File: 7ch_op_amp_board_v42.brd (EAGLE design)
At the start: 10.5 x 15.2 mm, 12 parts

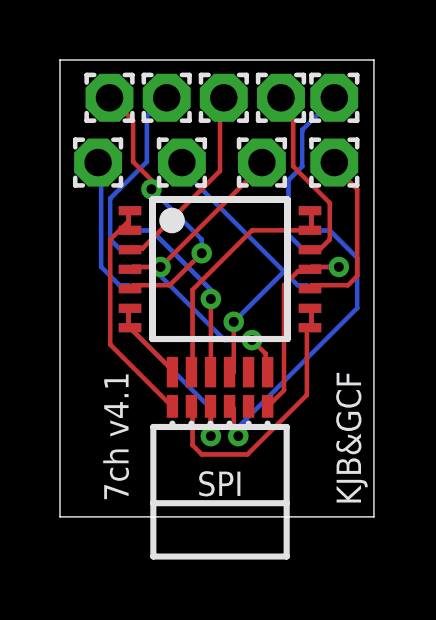
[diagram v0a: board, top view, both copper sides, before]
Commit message: Redraw traces to isolate power
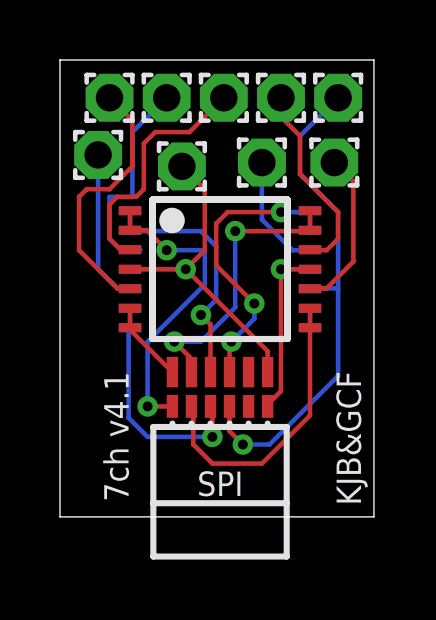
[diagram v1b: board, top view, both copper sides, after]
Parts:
- moved PAD8 5.64 mm to (9.27, 13.7)
- moved PAD7 3.24 mm to (6.73, 11.6)
- moved PAD9 2.67 mm to (4.06, 11.4)
- moved PAD5 0.25 mm to (1.27, 11.8)
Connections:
- net GND: now also SPI.B4; no longer SPI.T4
- net N$5: now also SPI.T4; no longer SPI.B4
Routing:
- net GND: track 10.4 -> 16.8 mm
- net N$1: track 7.96 -> 10.2 mm, vias 0 -> 2
- net N$21: track 6.11 -> 3.94 mm
- net N$5: track 11.4 -> 9.77 mm, vias 1 -> 3
- net N$8: track 6.64 -> 8.17 mm
- net N$3: track 6.40 -> 7.84 mm
- net N$4: track 6.95 -> 8.28 mm
- net N$7: track 8.19 -> 9.51 mm, vias 0 -> 2
- net N$9: track 9.02 -> 9.84 mm
- net N$22: track 6.33 -> 7.14 mm
- net V-: track 7.36 -> 6.73 mm
- net N$11: track 9.35 -> 8.83 mm, vias 2 -> 0
- net N$23: track 4.81 -> 5.32 mm
- net V+: track 12.6 -> 12.3 mm, vias 2 -> 1

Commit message: Cleanup files
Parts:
- moved PAD3 0.40 mm to (9.27, 11.9)
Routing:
- net N$5: track 9.77 -> 7.40 mm, vias 3 -> 1
- net N$21: track 3.94 -> 5.24 mm
- net GND: track 16.8 -> 17.9 mm
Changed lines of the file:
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@@
 <attribute name="VALUE" x="1.651" y="14.316" size="0.0254" layer="27"/>
 </element>
-<element name="PAD3" library="wirepad" package="1,6/0,9" value="" x="9.144" y="11.557" smashed="yes">
-<attribute name="VALUE" x="9.144" y="12.157" size="0.0254" layer="27"/>
+<element name="PAD3" library="wirepad" package="1,6/0,9" value="" x="9.271" y="11.938" smashed="yes">
+<attribute name="VALUE" x="9.271" y="12.538" size="0.0254" layer="27"/>
 </element>
 <element name="PAD4" library="wirepad" package="1,6/0,9" value="" x="7.366" y="13.716" smashed="yes">
@@
 <wire x1="5.6515" y1="5.5245" x2="5.715" y2="5.588" width="0.1524" layer="1"/>
 <via x="5.715" y="5.588" extent="1-16" drill="0.3302" diameter="0.254"/>
-<via x="6.477" y="6.858" extent="1-16" drill="0.3302" diameter="0.254"/>
-<via x="7.366" y="9.906" extent="1-16" drill="0.3302" diameter="0.254"/>
-<wire x1="7.366" y1="9.906" x2="8.289" y2="9.906" width="0.1524" layer="16"/>
+<wire x1="5.715" y1="5.588" x2="6.477" y2="6.35" width="0.1524" layer="16"/>
 <wire x1="8.289" y1="9.906" x2="8.334" y2="9.951" width="0.1524" layer="16"/>
-<wire x1="5.207" y1="8.128" x2="6.477" y2="6.858" width="0.1524" layer="1"/>
-<wire x1="6.477" y1="6.858" x2="6.477" y2="6.35" width="0.1524" layer="16"/>
-<wire x1="6.477" y1="6.35" x2="5.715" y2="5.588" width="0.1524" layer="16"/>
-<wire x1="7.366" y1="9.906" x2="5.588" y2="9.906" width="0.1524" layer="1"/>
-<wire x1="5.588" y1="9.906" x2="5.207" y2="9.525" width="0.1524" layer="1"/>
-<wire x1="5.207" y1="9.525" x2="5.207" y2="8.128" width="0.1524" layer="1"/>
+<wire x1="6.477" y1="8.89" x2="6.477" y2="6.35" width="0.1524" layer="16"/>
+<wire x1="6.477" y1="8.89" x2="6.858" y2="9.271" width="0.1524" layer="16"/>
+<wire x1="6.858" y1="9.271" x2="8.304" y2="9.271" width="0.1524" layer="16"/>
+<wire x1="8.304" y1="9.271" x2="8.334" y2="9.301" width="0.1524" layer="16"/>
 </signal>
 <signal name="N$9">
@@
 <wire x1="6.985" y1="2.159" x2="9.271" y2="4.445" width="0.1524" layer="16"/>
 <wire x1="9.271" y1="4.445" x2="9.271" y2="7.366" width="0.1524" layer="16"/>
-<wire x1="8.001" y1="12.446" x2="8.001" y2="11.176" width="0.1524" layer="16"/>
-<wire x1="8.001" y1="11.176" x2="9.271" y2="9.906" width="0.1524" layer="16"/>
-<wire x1="9.271" y1="9.906" x2="9.271" y2="7.366" width="0.1524" layer="16"/>
+<wire x1="9.779" y1="7.874" x2="9.271" y2="7.366" width="0.1524" layer="16"/>
+<wire x1="8.001" y1="12.446" x2="8.001" y2="11.557" width="0.1524" layer="16"/>
+<wire x1="9.779" y1="10.795" x2="9.779" y2="7.874" width="0.1524" layer="16"/>
+<wire x1="9.779" y1="10.795" x2="8.763" y2="10.795" width="0.1524" layer="16"/>
+<wire x1="8.763" y1="10.795" x2="8.001" y2="11.557" width="0.1524" layer="16"/>
 </signal>
 <signal name="N$1">
@@
 <contactref element="1" pad="10"/>
 <contactref element="PAD3" pad="1"/>
-<wire x1="9.144" y1="11.557" x2="9.779" y2="10.922" width="0.1524" layer="1"/>
-<wire x1="9.779" y1="10.922" x2="9.779" y2="8.255" width="0.1524" layer="1"/>
 <wire x1="9.779" y1="8.255" x2="8.89" y2="7.366" width="0.1524" layer="1"/>
 <wire x1="8.89" y1="7.366" x2="8.349" y2="7.366" width="0.1524" layer="1"/>
 <wire x1="8.349" y1="7.366" x2="8.334" y2="7.351" width="0.1524" layer="1"/>
+<wire x1="9.271" y1="11.938" x2="9.779" y2="11.43" width="0.1524" layer="1"/>
+<wire x1="9.779" y1="11.43" x2="9.779" y2="8.255" width="0.1524" layer="1"/>
 </signal>
 <signal name="N$13">
@@
 <contactref element="2" pad="10"/>
 <contactref element="PAD7" pad="1"/>
-<wire x1="6.731" y1="11.557" x2="6.731" y2="9.652" width="0.1524" layer="16"/>
-<wire x1="6.731" y1="9.652" x2="7.747" y2="8.636" width="0.1524" layer="16"/>
-<wire x1="7.747" y1="8.636" x2="8.319" y2="8.636" width="0.1524" layer="16"/>
 <wire x1="8.319" y1="8.636" x2="8.334" y2="8.651" width="0.1524" layer="16"/>
+<wire x1="6.731" y1="11.557" x2="7.874" y2="10.414" width="0.1524" layer="16"/>
+<wire x1="9.271" y1="9.017" x2="8.89" y2="8.636" width="0.1524" layer="16"/>
+<wire x1="8.89" y1="8.636" x2="8.349" y2="8.636" width="0.1524" layer="16"/>
+<wire x1="8.349" y1="8.636" x2="8.334" y2="8.651" width="0.1524" layer="16"/>
+<wire x1="7.874" y1="10.414" x2="8.763" y2="10.414" width="0.1524" layer="16"/>
+<wire x1="8.763" y1="10.414" x2="9.271" y2="9.906" width="0.1524" layer="16"/>
+<wire x1="9.271" y1="9.906" x2="9.271" y2="9.017" width="0.1524" layer="16"/>
 </signal>
 <signal name="N$22">
